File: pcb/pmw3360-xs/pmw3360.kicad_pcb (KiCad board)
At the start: 2 copper layers, 25 x 25 mm, 22 parts, among them IC1001 AP7335-WG-7, J1001 Conn_01x01_Socket, J1002 Conn_01x01_Socket, J1004 Conn_01x01_Socket, J1005 Conn_01x01_Socket, J1006 Conn_01x01_Socket, J1007 Conn_01x01_Socket, U1001 PMW3360DM-T2QU

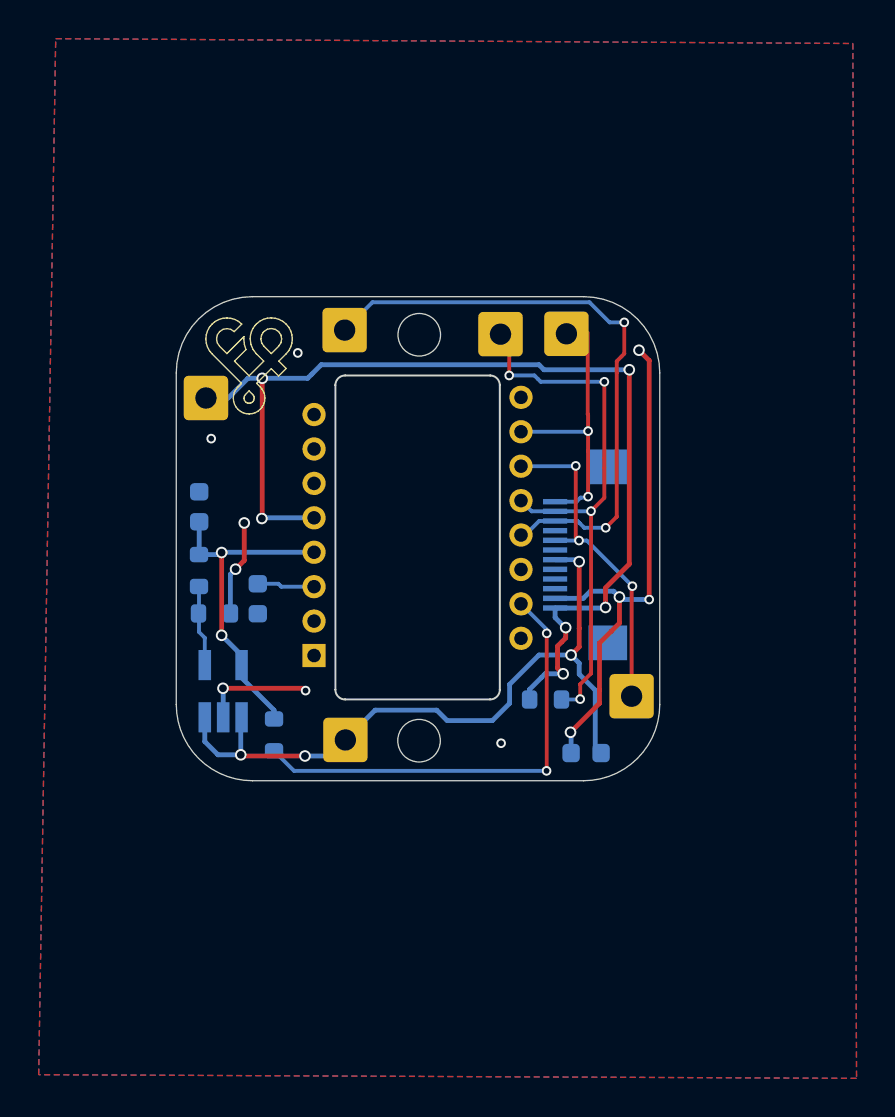
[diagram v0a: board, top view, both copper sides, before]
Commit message: moved mounting holes a bit so they don't interfere with the pmw3360 lens
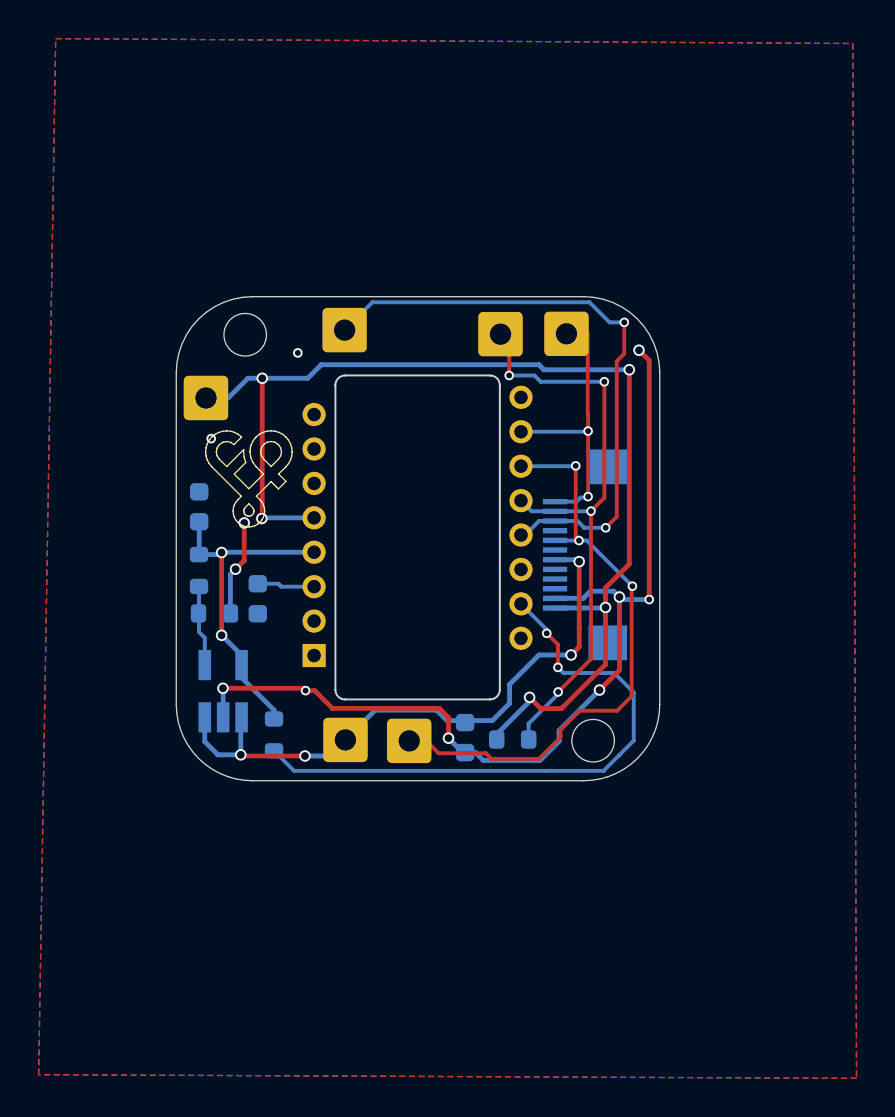
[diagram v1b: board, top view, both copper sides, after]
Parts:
- moved J1006 11.7 mm to (81.1, 121.2)
- moved REF** 9.00 mm to (72.6, 100.2)
- moved REF** 9.00 mm to (90.6, 121.2)
- moved C1002 6.31 mm to (84.0, 121.0), turned to -90 degrees
- moved REF** 5.84 mm to (72.8, 107.4) (x2)
- moved R1001 2.68 mm to (86.5, 121.1)
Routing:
- net GND: track 38.2 -> 53.5 mm
- net MOSI: track 17.5 -> 30.9 mm
- net Net-(U1001-LED_P): track 23.7 -> 30.7 mm
- net VDD_5V: track 37.7 -> 32.0 mm
- net VDD_3.3V: track 54.6 -> 59.0 mm, vias 6 -> 5
- net MISO: track 29.1 -> 31.4 mm

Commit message: added readmes for pmw3360 modules, and added silks for breakout for pmw3360-xs
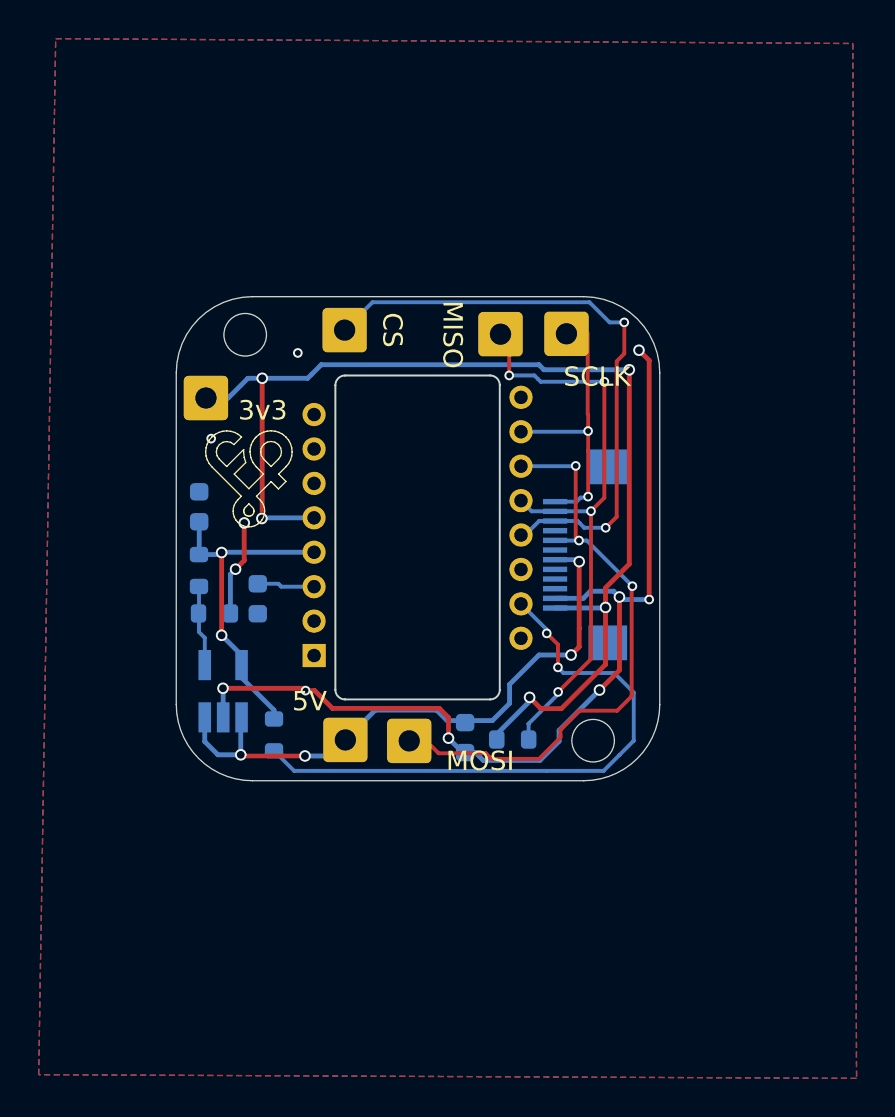
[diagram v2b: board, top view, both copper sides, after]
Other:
- board text added: "3v3"
- board text added: "5V"
- board text added: "CS"
- board text added: "MISO"
- board text added: "MOSI"
- board text added: "SCLK"
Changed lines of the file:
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@@
   (gr_arc (start 77.812 119.038001) (mid 77.458447 118.891554) (end 77.312 118.538001)
     (stroke (width 0.1) (type solid)) (layer "Edge.Cuts"))
+  (gr_text "MISO" (at 83.989194 98.392271 90) (layer "B.SilkS")
+    (effects (font (size 1 1) (thickness 0.15)) (justify left bottom mirror))
+  )
+  (gr_text "SCLK" (at 92.979194 102.952271) (layer "B.SilkS")
+    (effects (font (size 1 1) (thickness 0.15)) (justify left bottom mirror))
+  )
+  (gr_text "3v3" (at 75.009194 104.702271) (layer "B.SilkS")
+    (effects (font (size 1 1) (thickness 0.15)) (justify left bottom mirror))
+  )
+  (gr_text "CS" (at 80.899194 98.982271 90) (layer "B.SilkS")
+    (effects (font (size 1 1) (thickness 0.15)) (justify left bottom mirror))
+  )
+  (gr_text "5V" (at 77.089194 119.712271) (layer "B.SilkS")
+    (effects (font (size 1 1) (thickness 0.15)) (justify left bottom mirror))
+  )
+  (gr_text "CS" (at 79.669194 99.022271 -90) (layer "F.SilkS")
+    (effects (font (size 1 1) (thickness 0.15)) (justify left bottom))
+  )
+  (gr_text "MISO" (at 82.779194 98.402271 -90) (layer "F.SilkS")
+    (effects (font (size 1 1) (thickness 0.15)) (justify left bottom))
+  )
+  (gr_text "MOSI" (at 83.029194 122.812271) (layer "F.SilkS")
+    (effects (font (size 1 1) (thickness 0.15)) (justify left bottom))
+  )
+  (gr_text "SCLK" (at 89.099194 102.942271) (layer "F.SilkS")
+    (effects (font (size 1 1) (thickness 0.15)) (justify left bottom))
+  )
+  (gr_text "3v3" (at 72.279194 104.682271) (layer "F.SilkS")
+    (effects (font (size 1 1) (thickness 0.15)) (justify left bottom))
+  )
+  (gr_text "5V" (at 75.069194 119.722271) (layer "F.SilkS")
+    (effects (font (size 1 1) (thickness 0.15)) (justify left bottom))
+  )
   (segment (start 91.999194 117.522271) (end 91.999194 113.742271) (width 0.25) (layer "F.Cu") (net 1))
   (segment (start 72.149194 112.302271) (end 72.599194 111.852271) (width 0.25) (layer "F.Cu") (net 1))

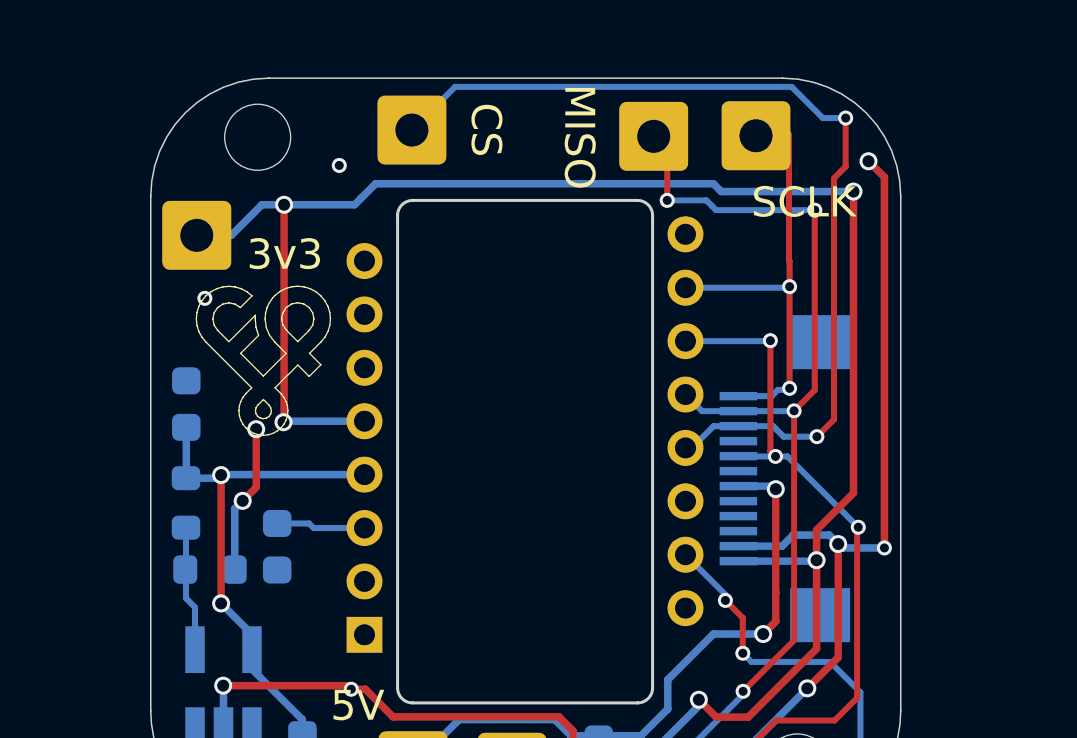
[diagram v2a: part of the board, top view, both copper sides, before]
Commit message: added ground through hole for vik pmw3360 xs
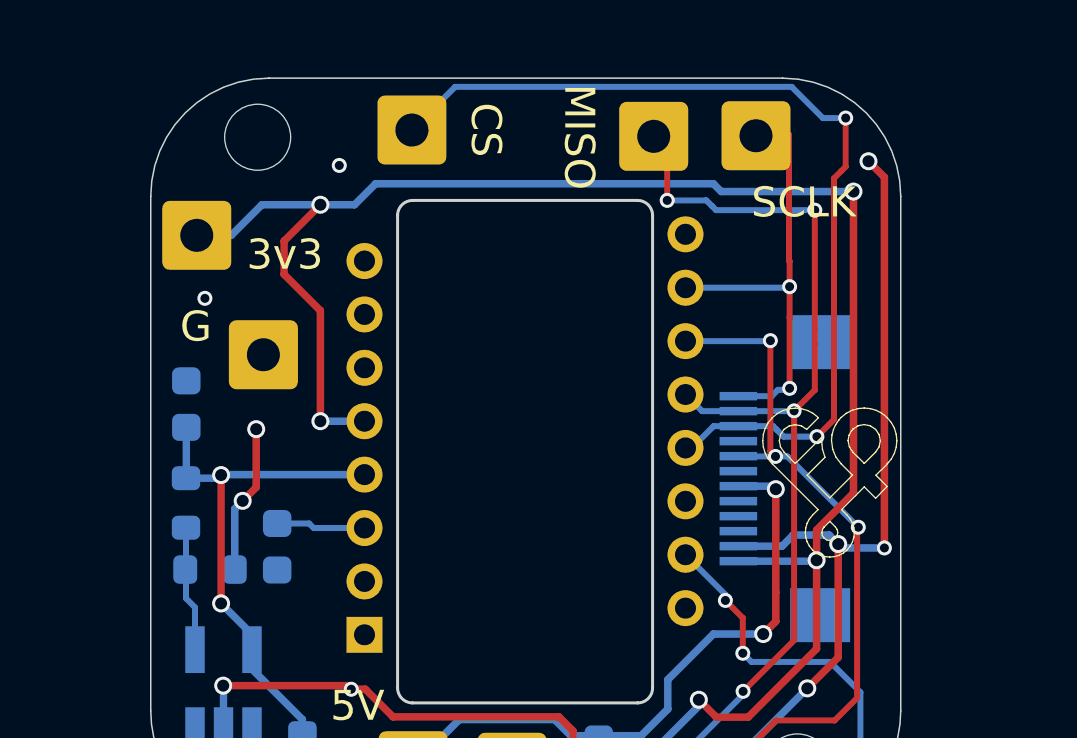
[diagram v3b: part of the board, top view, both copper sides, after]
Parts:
- removed the REF** at (72.8, 107.4)
- added J1008: Conn_01x01_Socket, Connector_Wire:SolderWire-0.5sqmm_1x01_D0.9mm_OD2.3mm, F.Cu at (72.8, 107.4)
- moved REF** 19.3 mm to (91.7, 111.5)
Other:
- board text added: "G"
